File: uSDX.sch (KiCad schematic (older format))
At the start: 21 parts

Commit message: a
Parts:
- removed R? (x2): 10k, symbol Device:R
- added C112, C116, C117: 100nF, symbol Device:C
- added C113, C115, C118: 10uF, symbol Device:C
- added C114: CP, symbol Device:CP
- added F101: Fuse, symbol Device:Fuse
- added J101: Jack-DC, symbol Connector:Jack-DC
- added L102, L103: 100uH, symbol Device:L
- added Q101, Q102: 2N7002, Package_TO_SOT_SMD:SOT-23, symbol Transistor_FET:2N7002
- added R103, R104, R105, R106: 4k7, symbol Device:R
- added U104: LD1117S50TR_SOT223, Package_TO_SOT_SMD:SOT-223-3_TabPin2, symbol Regulator_Linear:LD1117S50TR_SOT223
- added U105: LD1117S33TR_SOT223, Package_TO_SOT_SMD:SOT-223-3_TabPin2, symbol Regulator_Linear:LD1117S33TR_SOT223
- gave numbers to parts that had none: 19
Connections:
- net +3V3: now also L103.2, Q101.1 (G), Q102.1 (G), R103.1, R105.1
- net GND: now also C112.1, C113.1, C114.2, C115.1, C116.1, C117.1, C118.1, J101.2, U104.1 (GND), U105.1 (GND)
- net VCC: now also L102.2, R104.1, R106.1
- net SDA: now reaches U103.27 (PC4)
- net SDA: now also Q101.3 (D), R104.2
- net SCL: now reaches U103.28 (PC5)
- net SCL: now also Q102.3 (D), R106.2
- net at U101.4 (SCL): now also Q102.2 (S), R105.2
- net at U101.5 (SDA): now also Q101.2 (S), R103.2
- new net: C112.2, C113.2, L103.1, U105.2 (VO)
- new net: C117.2, C118.2, L102.1, U104.2 (VO), U105.3 (VI)
- new net +12V: C114.1, C115.2, C116.2, J101.1, U104.3 (VI)
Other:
- moved on the sheet: C101, C105, C106, R101, R102, U101, X101

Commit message: filter backup
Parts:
- removed C107: 100nF, symbol Device:C
- removed C109: 10nF, symbol Device:C
- removed U102: 74AHCT1G00, symbol 74xGxx:74AHCT1G00
- Y101: value Crystal -> 20MHz
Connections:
- net GND: now also C105.1
- net CLK0 renamed RF/CLK_I
- net CLK1 renamed RF/CLK_Q
- net CLK2 renamed RF/TX_CLK
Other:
- moved on the sheet: C101, C105, C106, Q101, Q102, R101, R102, R103, R104, R105, R106, U101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

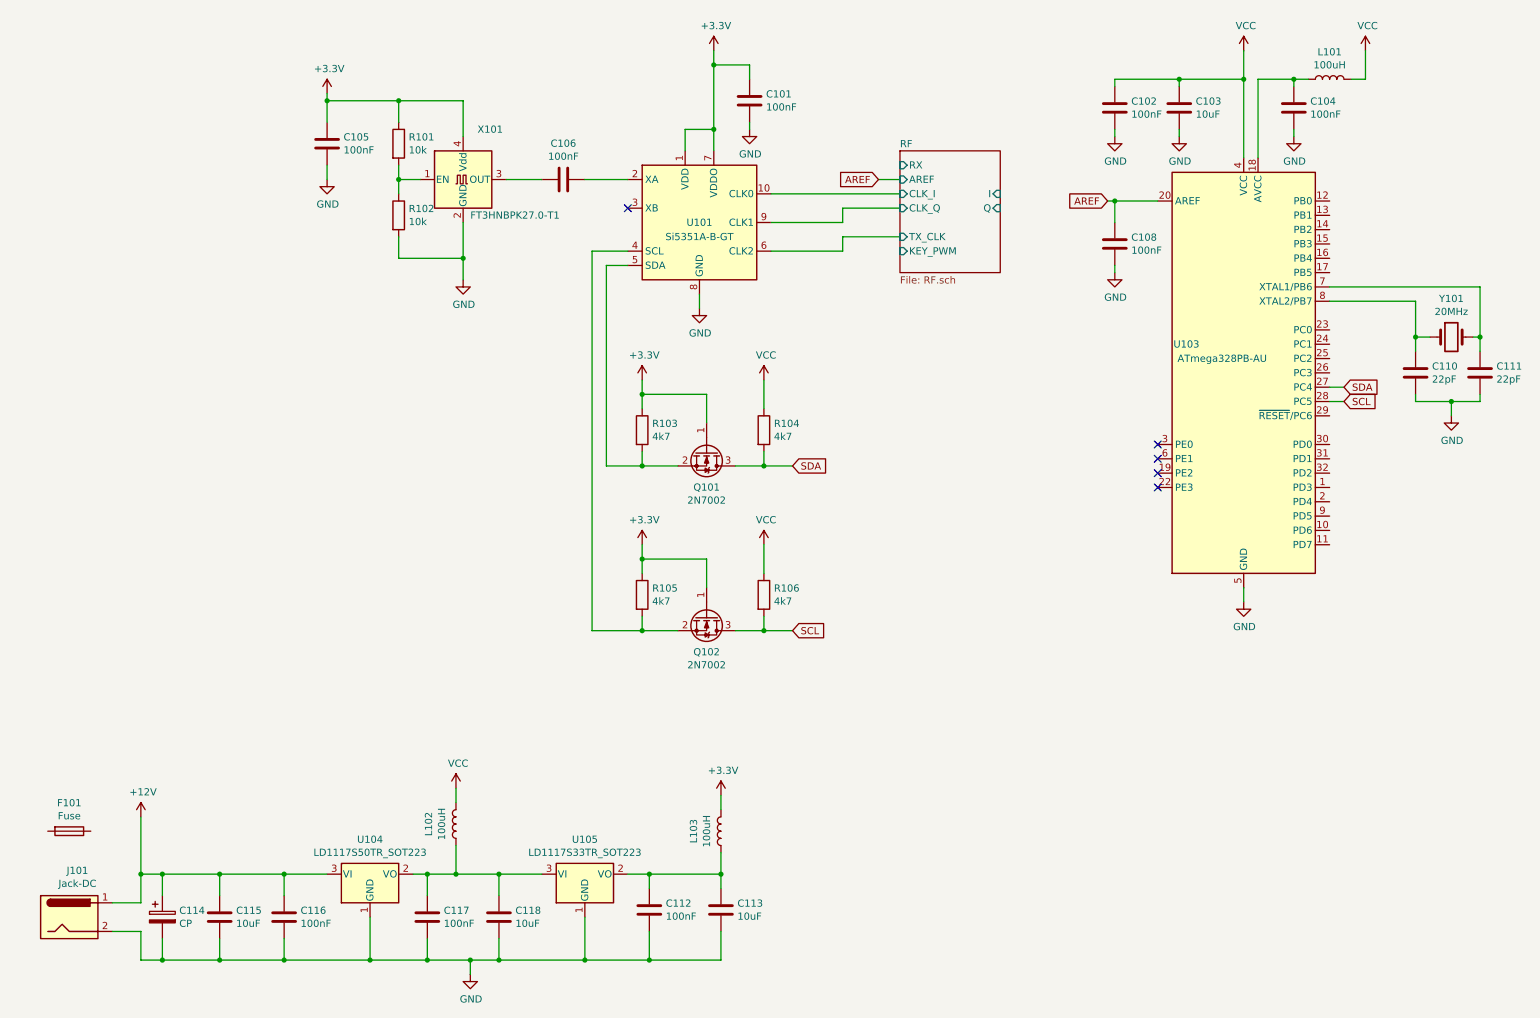
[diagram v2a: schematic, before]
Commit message: PCB in progress, filter screwed up
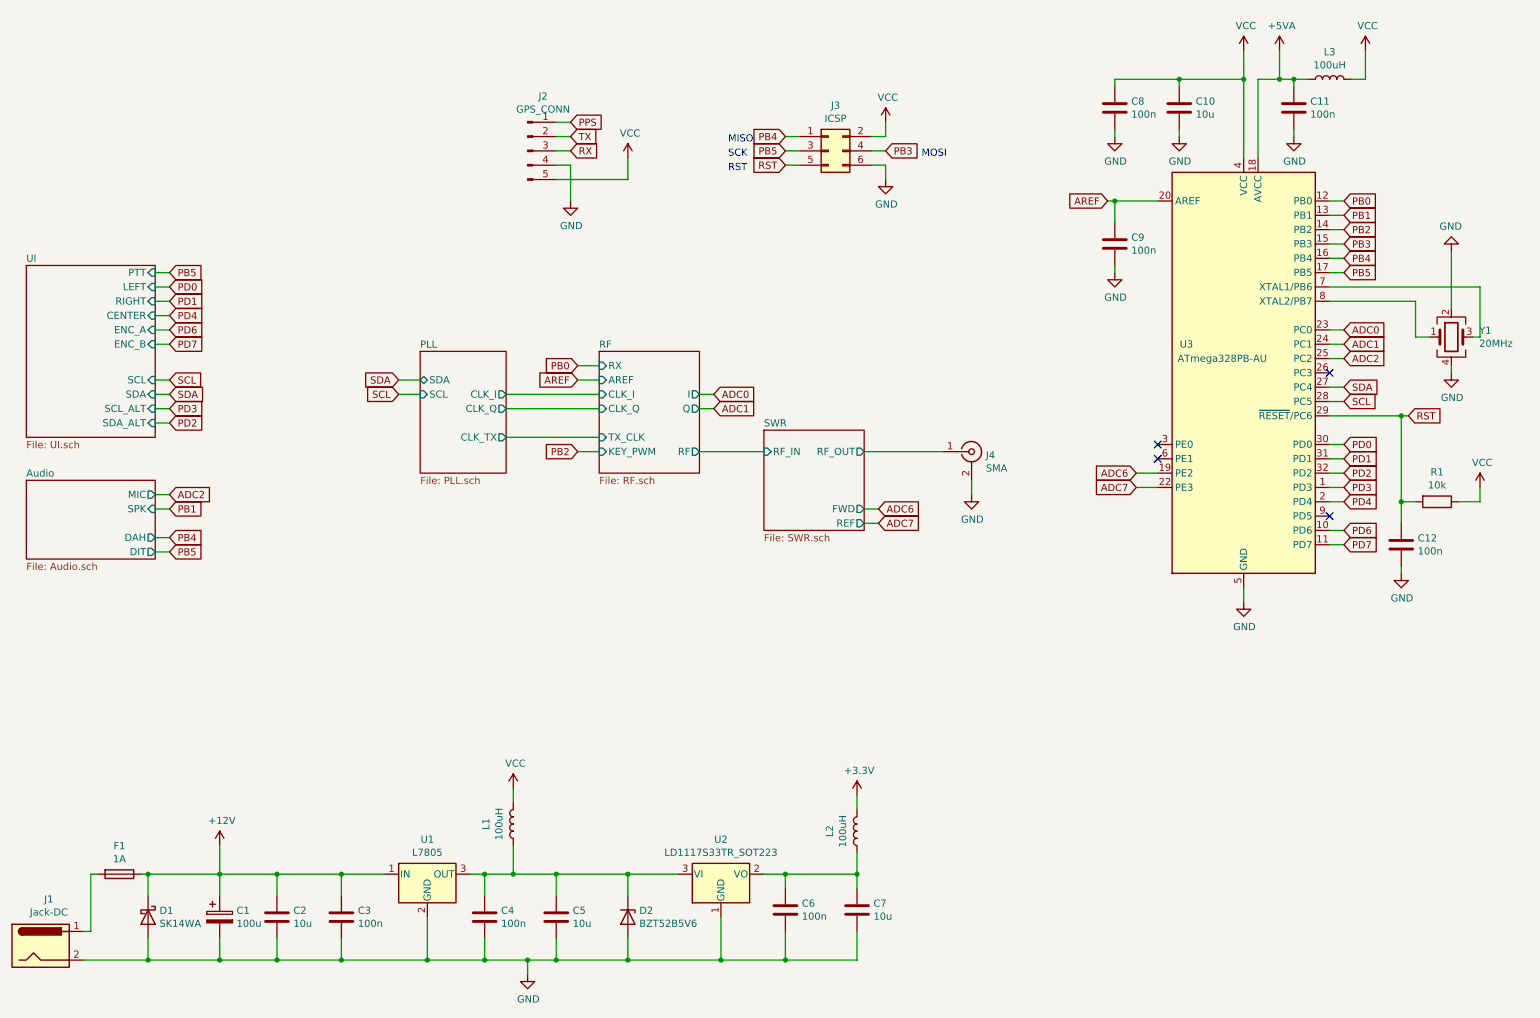
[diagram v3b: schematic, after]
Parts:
- removed C101, C105, C106: 100nF, symbol Device:C
- removed C110, C111: 22pF, symbol Device:C
- removed Q101, Q102: 2N7002, Package_TO_SOT_SMD:SOT-23, symbol Transistor_FET:2N7002
- removed R101, R102: 10k, symbol Device:R
- removed R103, R104, R105, R106: 4k7, symbol Device:R
- removed U101: Si5351A-B-GT, Package_SO:MSOP-10_3x3mm_P0.5mm, symbol Oscillator:Si5351A-B-GT
- removed U104: LD1117S50TR_SOT223, Package_TO_SOT_SMD:SOT-223-3_TabPin2, symbol Regulator_Linear:LD1117S50TR_SOT223
- removed X101: FT3HNBPK27.0-T1, Oscillator:Oscillator_SMD_Abracon_ASE-4Pin_3.2x2.5mm, symbol Oscillator:ASE-xxxMHz
- removed Y101: 20MHz, symbol Device:Crystal
- added C12: 100n, Capacitor_SMD:C_0805_2012Metric_Pad1.18x1.45mm_HandSolder, symbol Device:C
- added D1: SK14WA, Diode_SMD:D_SOD-123F, symbol Device:D_Schottky
- added D2: BZT52B5V6, Diode_SMD:D_SOD-123, symbol Diode:BZT52Bxx
- added J2: GPS_CONN, Connector_PinHeader_2.54mm:PinHeader_1x05_P2.54mm_Vertical, symbol Connector:Conn_01x05_Male
- added J3: ICSP, Connector_PinHeader_2.54mm:PinHeader_2x03_P2.54mm_Vertical, symbol Connector_Generic:Conn_02x03_Odd_Even
- added J4: SMA, Connector_Coaxial:SMA_Molex_73251-2120_EdgeMount_Horizontal, symbol Connector:Conn_Coaxial
- added R1: 10k, Resistor_SMD:R_0805_2012Metric_Pad1.20x1.40mm_HandSolder, symbol Device:R
- added U1: L7805, Package_TO_SOT_SMD:TO-252-2, symbol Regulator_Linear:L7805
- added Y1: 20MHz, Crystal:Crystal_SMD_3225-4Pin_3.2x2.5mm, symbol Device:Crystal_GND24
- C1: renamed from C114; value CP -> 100u; footprint (none) -> Capacitor_SMD:CP_Elec_6.3x7.7
- C10: renamed from C103; value 10uF -> 10u; footprint (none) -> Capacitor_SMD:C_0805_2012Metric_Pad1.18x1.45mm_HandSolder
- C11: renamed from C104; value 100nF -> 100n; footprint (none) -> Capacitor_SMD:C_0805_2012Metric_Pad1.18x1.45mm_HandSolder
- C2: renamed from C115; value 10uF -> 10u; footprint (none) -> Capacitor_SMD:C_0805_2012Metric_Pad1.18x1.45mm_HandSolder
- C3: renamed from C116; value 100nF -> 100n; footprint (none) -> Capacitor_SMD:C_0805_2012Metric_Pad1.18x1.45mm_HandSolder
- C4: renamed from C117; value 100nF -> 100n; footprint (none) -> Capacitor_SMD:C_0805_2012Metric_Pad1.18x1.45mm_HandSolder
- C5: renamed from C118; value 10uF -> 10u; footprint (none) -> Capacitor_SMD:C_0805_2012Metric_Pad1.18x1.45mm_HandSolder
- C6: renamed from C112; value 100nF -> 100n; footprint (none) -> Capacitor_SMD:C_0805_2012Metric_Pad1.18x1.45mm_HandSolder
- C7: renamed from C113; value 10uF -> 10u; footprint (none) -> Capacitor_SMD:C_0805_2012Metric_Pad1.18x1.45mm_HandSolder
- C8: renamed from C102; value 100nF -> 100n; footprint (none) -> Capacitor_SMD:C_0805_2012Metric_Pad1.18x1.45mm_HandSolder
- C9: renamed from C108; value 100nF -> 100n; footprint (none) -> Capacitor_SMD:C_0805_2012Metric_Pad1.18x1.45mm_HandSolder
- F1: renamed from F101; value Fuse -> 1A; footprint (none) -> Fuse:Fuse_0603_1608Metric_Pad1.05x0.95mm_HandSolder
- J1: renamed from J101; footprint (none) -> Connector_BarrelJack:BarrelJack_Wuerth_6941xx301002
- L1: renamed from L102; footprint (none) -> Inductor_SMD:L_0805_2012Metric_Pad1.15x1.40mm_HandSolder
- L2: renamed from L103; footprint (none) -> Inductor_SMD:L_0805_2012Metric_Pad1.15x1.40mm_HandSolder
- L3: renamed from L101; footprint (none) -> Inductor_SMD:L_0805_2012Metric_Pad1.15x1.40mm_HandSolder
- renumbered U105 to U2, U103 to U3
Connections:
- net +12V: now also F1.1, D1.1 (K), U1.1 (IN); no longer J1.1
- net GND: now also C12.1, D1.2 (A), D2.2 (A), J2.4 (Pin_4), J3.6 (Pin_6), J4.2 (Ext), U1.2 (GND), Y1.2, Y1.4
- net VCC: now also J2.5 (Pin_5), J3.2 (Pin_2), R1.1
- net PD3: now reaches U3.1 (PD3)
- net PD6: now reaches U3.10 (PD6)
- net PD7: now reaches U3.11 (PD7)
- net PB0: now reaches U3.12 (PB0)
- net PB1: now reaches U3.13 (PB1)
- net PB2: now reaches U3.14 (PB2)
- net PB3: now reaches U3.15 (PB3)
- net PB3: now also J3.4 (Pin_4)
- net PB4: now reaches U3.16 (PB4)
- net PB4: now also J3.1 (Pin_1)
- net PB5: now reaches U3.17 (PB5)
- net PB5: now also J3.3 (Pin_3)
- net +5VA: now reaches C11.2, L3.1, U3.18 (AVCC)
- net ADC6: now reaches U3.19 (PE2)
- net PD4: now reaches U3.2 (PD4)
- net ADC7: now reaches U3.22 (PE3)
- net ADC0: now reaches U3.23 (PC0)
- net ADC1: now reaches U3.24 (PC1)
- net ADC2: now reaches U3.25 (PC2)
- net RST: now reaches U3.29 (~RESET~/PC6)
- net RST: now also C12.2, J3.5 (Pin_5), R1.2
- net PD0: now reaches U3.30 (PD0)
- net PD1: now reaches U3.31 (PD1)
- net PD2: now reaches U3.32 (PD2)
- net at U3.7 (XTAL1/PB6): now also Y1.3
- net at U3.8 (XTAL2/PB7): now also Y1.1
- net at C4.2, C5.2, L1.1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: now also D2.1 (K), U1.3 (OUT)
- net at F1.2: now also J1.1
- new net PPS: J2.1 (Pin_1)
- new net RX: J2.3 (Pin_3)
- new net SWR/RF_OUT: J4.1 (In)
- new net TX: J2.2 (Pin_2)
- no-connect marks 5 -> 4
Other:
- note added: "MISO\n"
- note added: "MOSI"
- note added: "RST\n"
- note added: "SCK\n"
- moved on the sheet: C1, C2, C3, C4, C5, C6, C7, F1, J1, L1, L2, U2

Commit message: Almost final PCB
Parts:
- removed C12: 100n, Capacitor_SMD:C_0805_2012Metric_Pad1.18x1.45mm_HandSolder, symbol Device:C
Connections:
- net PD0 is gone; now on net RX: U3.30 (PD0)
- net PD1 is gone; now on net TX: U3.31 (PD1)
- net PPS is gone; now on net PD2: J2.1 (Pin_1)
- net PE0: now reaches U3.3 (PE0)
- net PD5: now reaches U3.9 (PD5)
- no-connect marks 4 -> 2
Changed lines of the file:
@@
 	1    0    0    -1
 $EndComp
-Text GLabel 4500 1350 2    50   Input ~ 0
-PPS
 Text GLabel 4500 1550 2    50   Input ~ 0
 RX
@@
 Wire Wire Line
 	6650 4150 6550 4150
-Text GLabel 9900 3600 2    50   Input ~ 0
-PD0
-Text GLabel 9900 3700 2    50   Input ~ 0
-PD1
 Text GLabel 9900 4000 2    50   Input ~ 0
 PD4
-Text GLabel 1700 2500 2    50   Input ~ 0
-PD0
-Text GLabel 1700 2600 2    50   Input ~ 0
-PD1
 Text GLabel 1700 2700 2    50   Input ~ 0
 PD4
@@
 Wire Wire Line
 	9800 4000 9900 4000
-NoConn ~ 8600 3600
 NoConn ~ 8600 3700
 Text GLabel 9900 2200 2    50   Input ~ 0
@@
 Connection ~ 10300 3400
 $Comp
-L Device:C C12
-U 1 1 60E67CD4
-P 10300 4300
-F 0 "C12" H 10185 4254 50  0000 R CNN
-F 1 "100n" H 10185 4345 50  0000 R CNN
-F 2 "Capacitor_SMD:C_0805_2012Metric_Pad1.18x1.45mm_HandSolder" H 10338 4150 50  0001 C CNN
-F 3 "~" H 10300 4300 50  0001 C CNN
-	1    10300 4300
-	-1   0    0    1
-$EndComp
-Wire Wire Line
-	10300 4150 10300 4000
-Connection ~ 10300 4000
-$Comp
-L power:GND #PWR018
-U 1 1 60E704DF
-P 10300 4500
-F 0 "#PWR018" H 10300 4250 50  0001 C CNN
-F 1 "GND" H 10305 4327 50  0000 C CNN
-F 2 "" H 10300 4500 50  0001 C CNN
-F 3 "" H 10300 4500 50  0001 C CNN
-	1    10300 4500
-	1    0    0    -1
-$EndComp
-Wire Wire Line
-	10300 4500 10300 4450
-NoConn ~ 9800 4100
-$Comp
 L Device:Crystal_GND24 Y1
 U 1 1 610588A8
@@
 Wire Wire Line
 	10650 2250 10650 2650
+Text GLabel 9900 3600 2    50   Input ~ 0
+RX
+Text GLabel 9900 3700 2    50   Input ~ 0
+TX
+Text GLabel 4500 1350 2    50   Input ~ 0
+PD2
+Text GLabel 9900 4100 2    50   Input ~ 0
+PD5
+Wire Wire Line
+	9900 4100 9800 4100
+Text GLabel 1700 2600 2    50   Input ~ 0
+PD5
+Text GLabel 8450 3600 0    50   Input ~ 0
+PE0
+Wire Wire Line
+	8450 3600 8600 3600
+Text GLabel 1700 2500 2    50   Input ~ 0
+PE0
 $EndSCHEMATC
